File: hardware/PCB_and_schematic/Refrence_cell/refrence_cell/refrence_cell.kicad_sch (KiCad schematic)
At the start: 52 parts, among them J1 ICP_DEBUG, J2 DS18B20, J3 DS18B20, J4 DS18B20, J5 RS485, J6 Conn_01x02, J7 Conn_01x02, Q1 BC817, Q2 BC327, Q3 BC337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

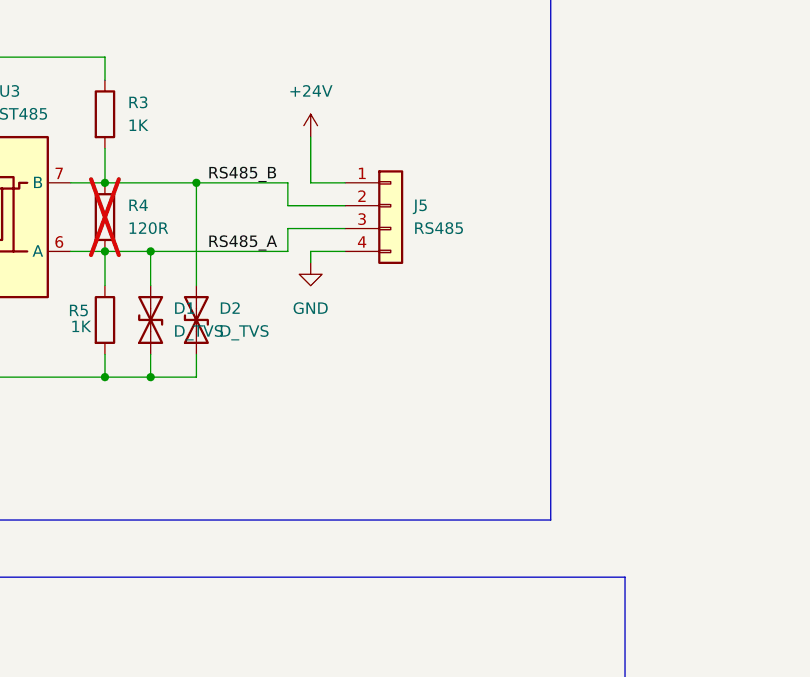
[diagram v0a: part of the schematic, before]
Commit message: add refrence cell pcb
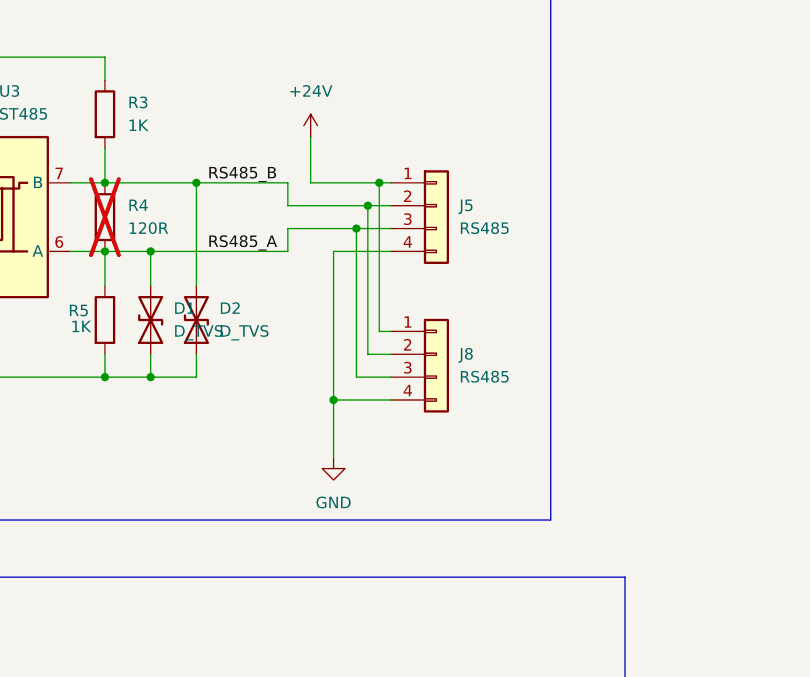
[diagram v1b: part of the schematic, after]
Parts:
- added J8: RS485, My-Footprints-connectors:PinHeader_1x04_P2.54mm_Vertical_littleBigger, symbol Connector_Generic:Conn_01x04
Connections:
- net +24V: now also J8.1 (Pin_1)
- net GND: now also J8.4 (Pin_4)
- net RS485_A: now also J8.3 (Pin_3)
- net RS485_B: now also J8.2 (Pin_2)
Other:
- moved on the sheet: J5
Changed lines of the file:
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@@
 	)
 	(junction
+		(at 246.38 46.99)
+		(diameter 0)
+		(color 0 0 0 0)
+	)
+	(junction
 		(at 54.61 180.34)
 		(diameter 0)
@@
 	)
 	(junction
+		(at 242.57 68.58)
+		(diameter 0)
+		(color 0 0 0 0)
+	)
+	(junction
 		(at 203.2 30.48)
 		(diameter 0)
@@
 	)
 	(junction
+		(at 247.65 44.45)
+		(diameter 0)
+		(color 0 0 0 0)
+	)
+	(junction
 		(at 81.28 190.5)
 		(diameter 0)
@@
 	)
 	(junction
+		(at 245.11 49.53)
+		(diameter 0)
+		(color 0 0 0 0)
+	)
+	(junction
 		(at 97.79 250.19)
 		(diameter 0)
@@
 	(wire
 		(pts
+			(xy 248.92 63.5) (xy 246.38 63.5)
+		)
+		(stroke
+			(width 0)
+			(type default)
+		)
+	)
+	(wire
+		(pts
 			(xy 217.17 33.02) (xy 217.17 30.48)
 		)
@@
 	(wire
 		(pts
+			(xy 245.11 49.53) (xy 248.92 49.53)
+		)
+		(stroke
+			(width 0)
+			(type default)
+		)
+	)
+	(wire
+		(pts
 			(xy 240.03 39.37) (xy 240.03 44.45)
 		)
@@
 	(wire
 		(pts
-			(xy 243.84 44.45) (xy 240.03 44.45)
+			(xy 248.92 44.45) (xy 247.65 44.45)
 		)
 		(stroke
@@
 	(wire
 		(pts
+			(xy 248.92 60.96) (xy 247.65 60.96)
+		)
+		(stroke
+			(width 0)
+			(type default)
+		)
+	)
+	(wire
+		(pts
 			(xy 125.73 62.23) (xy 134.62 62.23)
 		)
@@
 	(wire
 		(pts
+			(xy 248.92 66.04) (xy 245.11 66.04)
+		)
+		(stroke
+			(width 0)
+			(type default)
+		)
+	)
+	(wire
+		(pts
 			(xy 54.61 191.77) (xy 54.61 193.04)
 		)
@@
 	(wire
 		(pts
+			(xy 246.38 63.5) (xy 246.38 46.99)
+		)
+		(stroke
+			(width 0)
+			(type default)
+		)
+	)
+	(wire
+		(pts
 			(xy 212.09 198.12) (xy 212.09 199.39)
 		)
@@
 	(wire
 		(pts
-			(xy 240.03 53.34) (xy 240.03 52.07)
+			(xy 242.57 74.93) (xy 242.57 68.58)
 		)
 		(stroke
@@
 	(wire
 		(pts
+			(xy 245.11 66.04) (xy 245.11 49.53)
+		)
+		(stroke
+			(width 0)
+			(type default)
+		)
+	)
+	(wire
+		(pts
 			(xy 50.8 67.31) (xy 59.69 67.31)
 		)
@@
 	(wire
 		(pts
-			(xy 240.03 52.07) (xy 243.84 52.07)
+			(xy 242.57 52.07) (xy 248.92 52.07)
 		)
 		(stroke
@@
 	(wire
 		(pts
-			(xy 237.49 49.53) (xy 243.84 49.53)
+			(xy 237.49 49.53) (xy 245.11 49.53)
 		)
 		(stroke
@@
 	(wire
 		(pts
+			(xy 242.57 68.58) (xy 242.57 52.07)
+		)
+		(stroke
+			(width 0)
+			(type default)
+		)
+	)
+	(wire
+		(pts
 			(xy 241.3 119.38) (xy 250.19 119.38)
 		)
@@
 	(wire
 		(pts
-			(xy 237.49 46.99) (xy 243.84 46.99)
+			(xy 237.49 46.99) (xy 246.38 46.99)
 		)
 		(stroke
@@
 	(wire
 		(pts
+			(xy 242.57 68.58) (xy 248.92 68.58)
+		)
+		(stroke
+			(width 0)
+			(type default)
+		)
+	)
+	(wire
+		(pts
+			(xy 247.65 60.96) (xy 247.65 44.45)
+		)
+		(stroke
+			(width 0)
+			(type default)
+		)
+	)
+	(wire
+		(pts
 			(xy 120.65 114.3) (xy 120.65 116.84)
 		)
@@
 	(wire
 		(pts
+			(xy 246.38 46.99) (xy 248.92 46.99)
+		)
+		(stroke
+			(width 0)
+			(type default)
+		)
+	)
+	(wire
+		(pts
 			(xy 54.61 180.34) (xy 59.69 180.34)
 		)
@@
 	(wire
 		(pts
+			(xy 247.65 44.45) (xy 240.03 44.45)
+		)
+		(stroke
+			(width 0)
+			(type default)
+		)
+	)
+	(wire
+		(pts
 			(xy 110.49 182.88) (xy 110.49 184.15)
 		)
@@
 	(symbol
 		(lib_id "power:GND")
-		(at 240.03 53.34 0)
+		(at 242.57 74.93 0)
 		(unit 1)
 		(exclude_from_sim no)
@@
 		(dnp no)
 		(property "Reference" "#PWR016"
-			(at 240.03 59.69 0)
+			(at 242.57 81.28 0)
 			(effects
 				(font
@@
 		)
 		(property "Value" "GND"
-			(at 240.03 58.42 0)
+			(at 242.57 80.01 0)
 			(effects
 				(font
@@
 		)
 		(property "Footprint" ""
-			(at 240.03 53.34 0)
+			(at 242.57 74.93 0)
 			(effects
 				(font
@@
 		)
 		(property "Datasheet" ""
-			(at 240.03 53.34 0)
+			(at 242.57 74.93 0)
 			(effects
 				(font
@@
 		)
 		(property "Description" "Power symbol creates a global label with name \"GND\" , ground"
-			(at 240.03 53.34 0)
+			(at 242.57 74.93 0)
 			(effects
 				(font
@@
 	)
 	(symbol
+		(lib_id "Connector_Generic:Conn_01x04")
+		(at 254 63.5 0)
+		(unit 1)
+		(exclude_from_sim no)
+		(in_bom yes)
+		(on_board yes)
+		(dnp no)
+		(fields_autoplaced yes)
+		(property "Reference" "J8"
+			(at 256.54 63.4999 0)
+			(effects
+				(font
+					(size 1.27 1.27)
+				)
+				(justify left)
+			)
+		)
+		(property "Value" "RS485"
+			(at 256.54 66.0399 0)
+			(effects
+				(font
+					(size 1.27 1.27)
+				)
+				(justify left)
+			)
+		)
+		(property "Footprint" "My-Footprints-connectors:PinHeader_1x04_P2.54mm_Vertical_littleBigger"
+			(at 254 63.5 0)
+			(effects
+				(font
+					(size 1.27 1.27)
+				)
+				(hide yes)
+			)
+		)
+		(property "Datasheet" "~"
+			(at 254 63.5 0)
+			(effects
+				(font
+					(size 1.27 1.27)
+				)
+				(hide yes)
+			)
+		)
+		(property "Description" "Generic connector, single row, 01x04, script generated (kicad-library-utils/schlib/autogen/connector/)"
+			(at 254 63.5 0)
+			(effects
+				(font
+					(size 1.27 1.27)
+				)
+				(hide yes)
+			)
+		)
+		(pin "3"
+		)
+		(pin "2"
+		)
+		(pin "4"
+		)
+		(pin "1"
+		)
+		(instances
+			(project "refrence_cell"
+				(path "/1700b202-8f4f-48fb-8169-decdd6437413"
+					(reference "J8")
+					(unit 1)
+				)
+			)
+		)
+	)
+	(symbol
 		(lib_id "Transistor_BJT:BC817")
 		(at 209.55 214.63 0)
@@
 	(symbol
 		(lib_id "Connector_Generic:Conn_01x04")
-		(at 248.92 46.99 0)
+		(at 254 46.99 0)
 		(unit 1)
 		(exclude_from_sim no)
@@
 		(fields_autoplaced yes)
 		(property "Reference" "J5"
-			(at 251.46 46.9899 0)
+			(at 256.54 46.9899 0)
 			(effects
 				(font
@@
 		)
 		(property "Value" "RS485"
-			(at 251.46 49.5299 0)
+			(at 256.54 49.5299 0)
 			(effects
 				(font
@@
 		)
 		(property "Footprint" "Connector_JST:JST_XA_B04B-XASK-1_1x04_P2.50mm_Vertical"
-			(at 248.92 46.99 0)
+			(at 254 46.99 0)
 			(effects
 				(font
@@
 		)
 		(property "Datasheet" "~"
-			(at 248.92 46.99 0)
+			(at 254 46.99 0)
 			(effects
 				(font
@@
 		)
 		(property "Description" "Generic connector, single row, 01x04, script generated (kicad-library-utils/schlib/autogen/connector/)"
-			(at 248.92 46.99 0)
+			(at 254 46.99 0)
 			(effects
 				(font

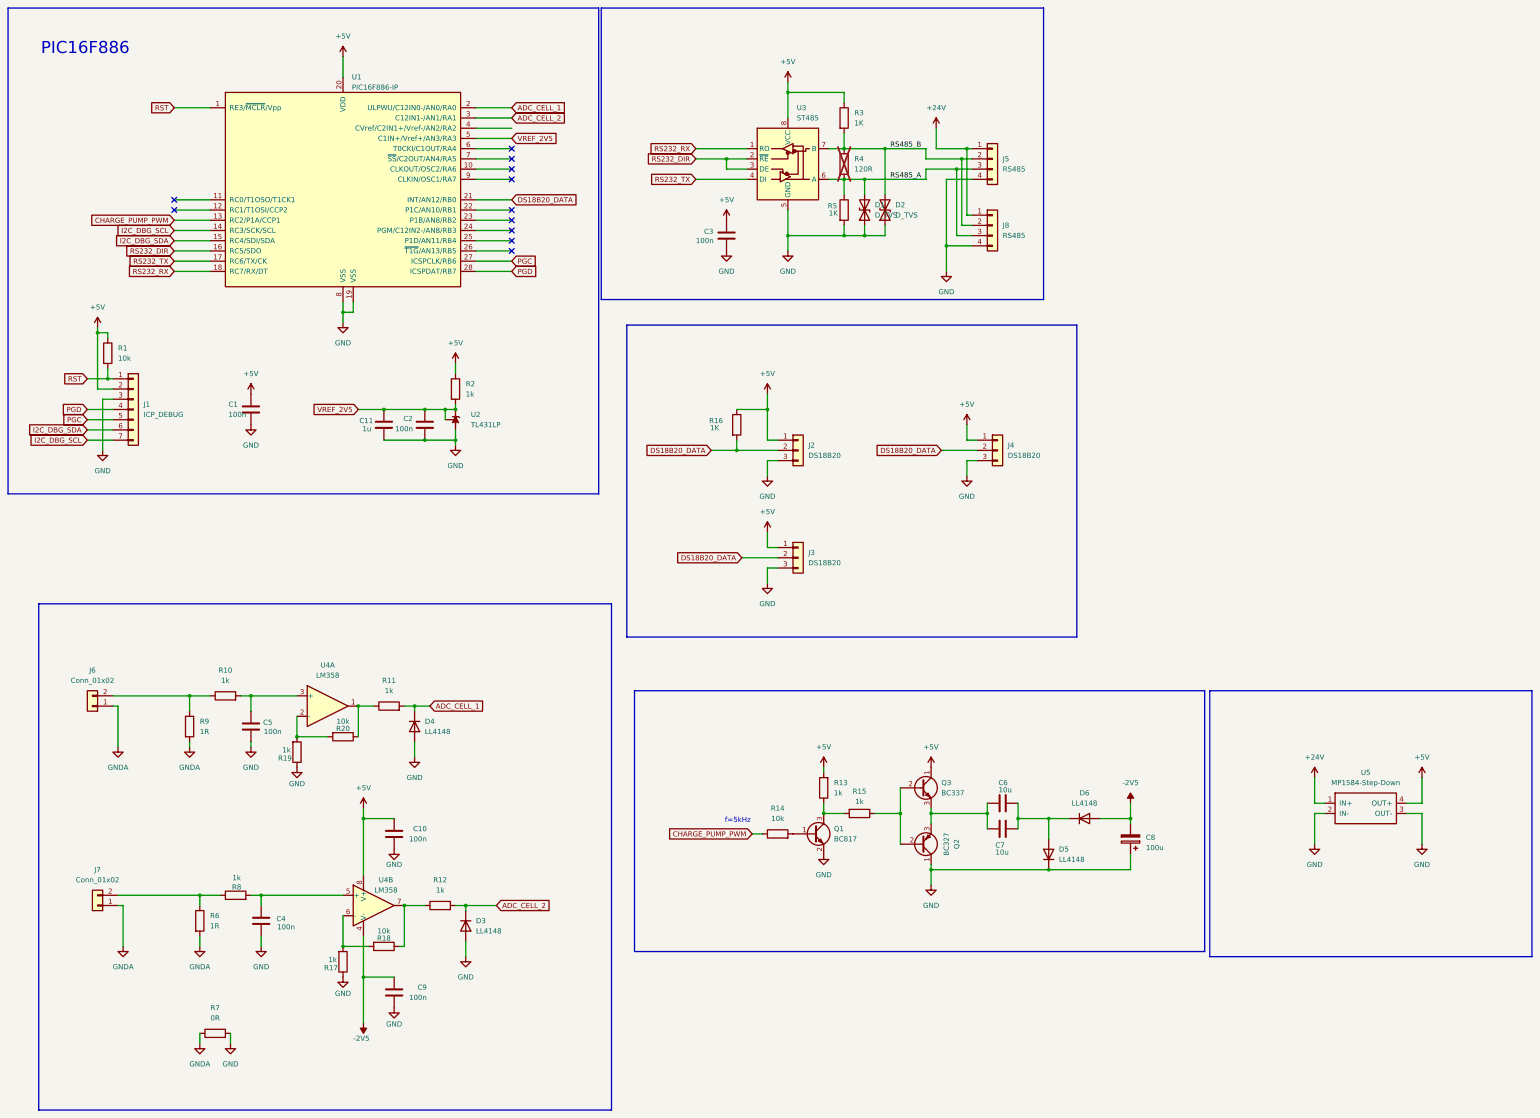
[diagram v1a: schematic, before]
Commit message: add balancer power module
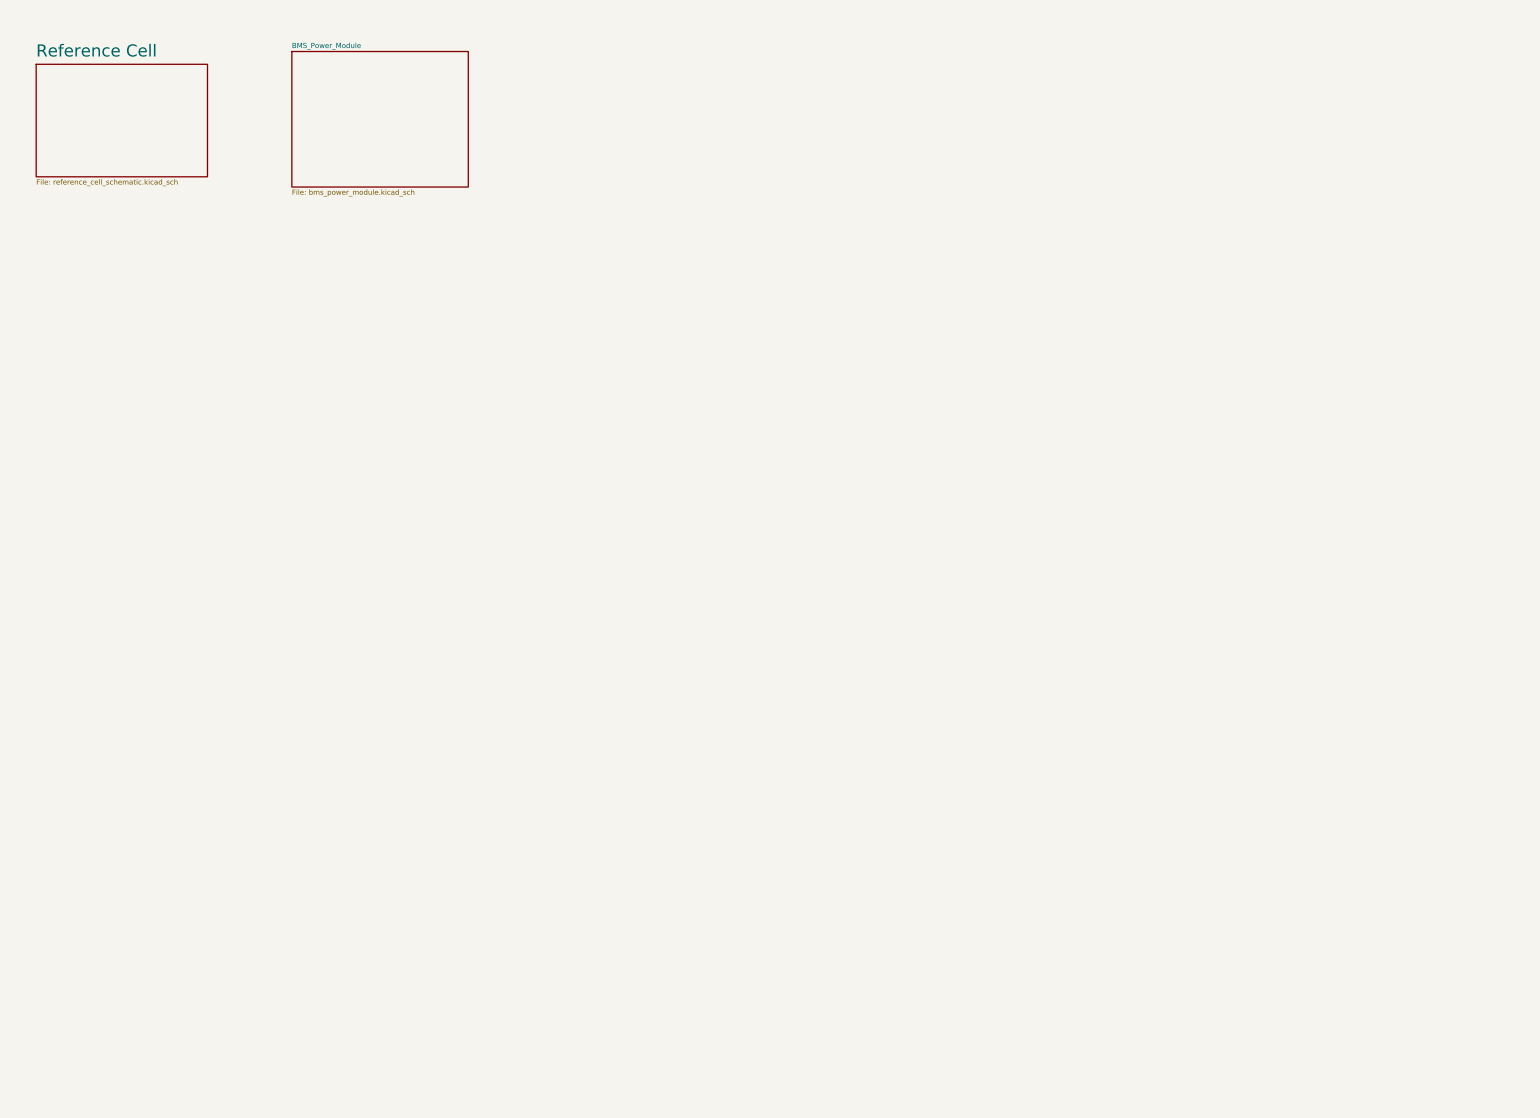
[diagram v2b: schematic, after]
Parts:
- removed C1, C10, C2, C3, C4, C5, C9: 100n, Capacitor_SMD:C_0805_2012Metric_Pad1.18x1.45mm_HandSolder, symbol Device:C
- removed C11: 1u, Capacitor_SMD:C_0805_2012Metric_Pad1.18x1.45mm_HandSolder, symbol Device:C
- removed C6, C7: 10u, Capacitor_SMD:C_1206_3216Metric_Pad1.33x1.80mm_HandSolder, symbol Device:C
- removed C8: 100u, Capacitor_THT:CP_Radial_D5.0mm_P2.50mm, symbol Device:C_Polarized
- removed D1, D2: D_TVS, Diode_SMD:D_SMA, symbol Device:D_TVS
- removed D3, D4: LL4148, Diode_SMD:D_MiniMELF, symbol Diode:LL4148
- removed D5, D6: LL4148, Diode_THT:D_DO-35_SOD27_P7.62mm_Horizontal, symbol Diode:LL4148
- removed J1: ICP_DEBUG, Connector_PinHeader_2.54mm:PinHeader_1x07_P2.54mm_Vertical, symbol Connector_Generic:Conn_01x07
- removed J2, J3, J4: DS18B20, Connector_JST:JST_XA_B03B-XASK-1_1x03_P2.50mm_Vertical, symbol Connector_Generic:Conn_01x03
- removed J5: RS485, Connector_JST:JST_XA_B04B-XASK-1_1x04_P2.50mm_Vertical, symbol Connector_Generic:Conn_01x04
- removed J6, J7: Conn_01x02, Connector_JST:JST_XA_B02B-XASK-1_1x02_P2.50mm_Vertical, symbol Connector_Generic:Conn_01x02
- removed J8: RS485, My-Footprints-connectors:PinHeader_1x04_P2.54mm_Vertical_littleBigger, symbol Connector_Generic:Conn_01x04
- removed Q1: BC817, Package_TO_SOT_SMD:SOT-23, symbol Transistor_BJT:BC817
- removed Q2: BC327, Package_TO_SOT_THT:TO-92_Inline, symbol Transistor_BJT:BC327
- removed Q3: BC337, Package_TO_SOT_THT:TO-92_Inline, symbol Transistor_BJT:BC337
- removed R1, R14, R18, R20: 10k, Resistor_SMD:R_0805_2012Metric_Pad1.20x1.40mm_HandSolder, symbol Device:R
- removed R10, R11, R12, R13, R15, R17, R19, R2, R8: 1k, Resistor_SMD:R_0805_2012Metric_Pad1.20x1.40mm_HandSolder, symbol Device:R
- removed R16, R3, R5: 1K, Resistor_SMD:R_0805_2012Metric_Pad1.20x1.40mm_HandSolder, symbol Device:R
- removed R4: 120R, Resistor_SMD:R_0805_2012Metric_Pad1.20x1.40mm_HandSolder, symbol Device:R
- removed R6, R9: 1R, Resistor_SMD:R_0805_2012Metric_Pad1.20x1.40mm_HandSolder, symbol Device:R
- removed R7: 0R, Resistor_SMD:R_0805_2012Metric_Pad1.20x1.40mm_HandSolder, symbol Device:R
- removed U1: PIC16F886-IP, Package_SO:SOIC-28W_7.5x17.9mm_P1.27mm, symbol MCU_Microchip_PIC16:PIC16F886-IP
- removed U2: TL431LP, My-Footprints:TO-92_Inline_LITTLE_BIGGER, symbol Reference_Voltage:TL431LP
- removed U3: ST485, Package_SO:SOIC-8_3.9x4.9mm_P1.27mm, symbol Interface_UART:ST485EBDR
- removed U4: LM358, Package_DIP:DIP-8_W7.62mm_LongPads, symbol Amplifier_Operational:LM358
- removed U5: MP1584-Step-Down, My-Footprints-converters-modules:MP1584_Mini_3A_Step_Down_Conv, symbol My-Lib:MP1584-Step-Down
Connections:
- no-connect marks 11 -> 0
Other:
- added sheet BMS_Power_Module (bms_power_module.kicad_sch)
- added sheet Reference Cell (reference_cell_schematic.kicad_sch)
- note removed: "PIC16F886"
- note removed: "f=5kHz"

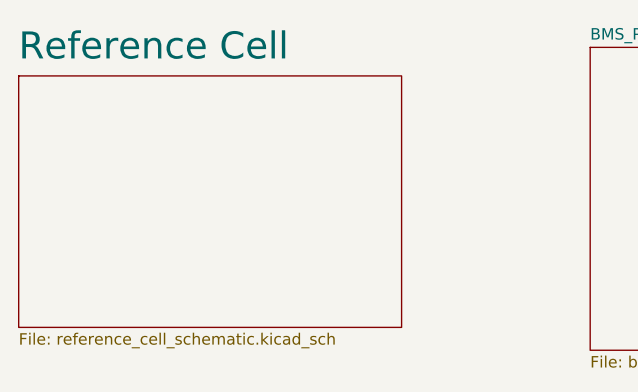
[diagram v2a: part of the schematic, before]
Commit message: routing power module
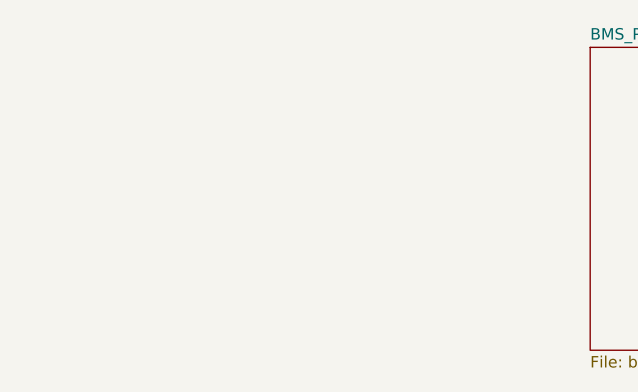
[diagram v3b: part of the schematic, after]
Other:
- removed sheet Reference Cell
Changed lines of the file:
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@@
 	(paper "A5")
-	(sheet
-		(at 16.51 23.495)
-		(size 42.545 27.94)
-		(fields_autoplaced yes)
-		(stroke
-			(width 0.1524)
-			(type solid)
-		)
-		(fill
-			(color 0 0 0 0.0000)
-		)
-		(property "Sheetname" "Reference Cell"
-			(at 16.51 21.9184 0)
-			(effects
-				(font
-					(size 3 3)
-				)
-				(justify left bottom)
-			)
-		)
-		(property "Sheetfile" "reference_cell_schematic.kicad_sch"
-			(at 16.51 52.0196 0)
-			(effects
-				(font
-					(size 1.27 1.27)
-				)
-				(justify left top)
-			)
-		)
-		(instances
-			(project "refrence_cell"
-				(path "/1700b202-8f4f-48fb-8169-decdd6437413"
-					(page "2")
-				)
-			)
-		)
-	)
 	(sheet
 		(at 80.01 20.32)
